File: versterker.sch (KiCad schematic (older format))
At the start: 4 parts, among them J1 J_Barreljack_3.5mm_Wurth_TH

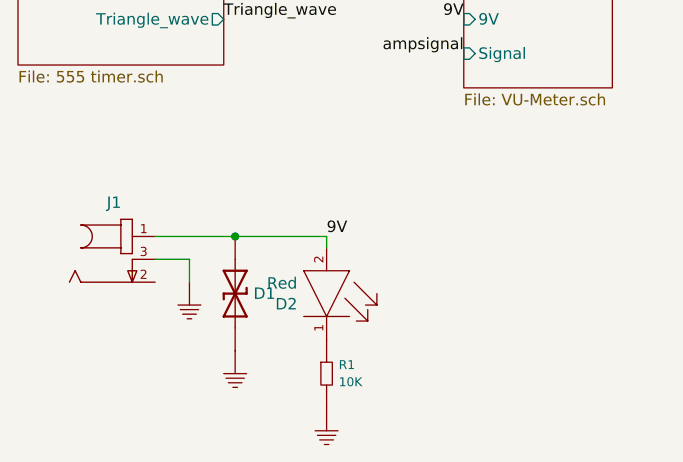
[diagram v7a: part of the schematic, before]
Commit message: changed partnumbers
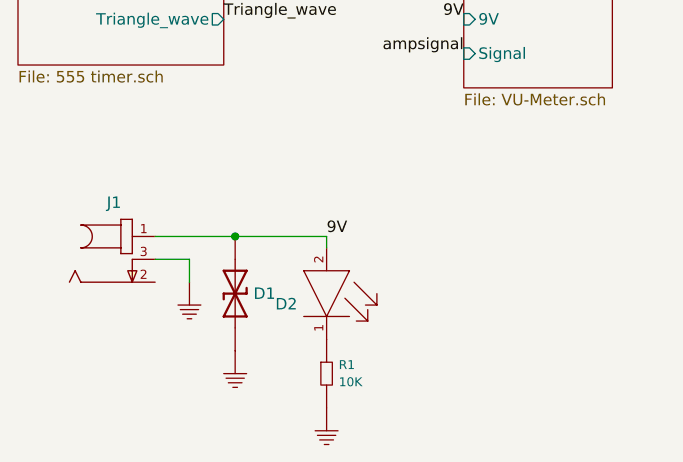
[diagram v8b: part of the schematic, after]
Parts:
- D2: Mouser (none) -> 710-150060RS75000; automotive No -> (none); category Diode -> (none); colour Red -> (none); device class L1 Optoelectronics -> (none); device class L2 LEDs -> (none); device class L3 unset -> (none); digikey description LED RED CLEAR 0603 SMD -> (none); digikey part number 732-4978-1-ND -> (none); forward current 20mA -> (none); forward voltage 2V -> (none); height 0.8mm -> (none); lead free Yes -> (none); led orientation Top View -> (none); library id cd4e03a66a96d806 -> (none); luminous intensity 250mcd -> (none); manufacturer Wurth -> (none); max junction temp +95°C -> (none); mouser description Standard LEDs - SMD WL-SMCW SMDMono TpVw Waterclr 0603 Red -> (none); mouser part number 710-150060RS75000 -> (none); package 0603 -> (none); peak emmision wavelength 630nm -> (none); power dissipation 72mW -> (none); reverse voltage 5V -> (none); rohs Yes -> (none); standoff height 0mm -> (none); temperature range high +85°C -> (none); temperature range low -40°C -> (none); viewing angle 140° -> (none); wavelength 625nm -> (none)
- R1: Digi-key YAG1236CT-ND -> (none); Mouser (none) -> 667-ERJ-UP3F1002V
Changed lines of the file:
@@
 F 2 "MAIN_PCB_LIB:D_9V_TVS_SMCJ-Q" H 3100 4050 50  0001 L BNN
 F 3 "" H 3100 4050 50  0001 L BNN
-F 4 "IPC-7351B" H 3100 4050 50  0001 L BNN "STANDARD"
-F 5 "Diodes Incorporated" H 3100 4050 50  0001 L BNN "MANUFACTURER"
-F 6 "2.62mm" H 3100 4050 50  0001 L BNN "MAXIMUM_PACKAGE_HEIGHT"
-F 7 "11/20/15" H 3100 4050 50  0001 L BNN "PARTREV"
-F 8 "576-SMCJ9.0CA" H 3100 4050 50  0001 C CNN "Mouser"
+F 4 "576-SMCJ9.0CA" H 3100 4050 50  0001 C CNN "Mouser"
+F 5 "Diodes Incorporated" H 0   0   50  0001 C CNN "MANUFACTURER"
+F 6 "2.62mm" H 0   0   50  0001 C CNN "MAXIMUM_PACKAGE_HEIGHT"
+F 7 "11/20/15" H 0   0   50  0001 C CNN "PARTREV"
+F 8 "IPC-7351B" H 0   0   50  0001 C CNN "STANDARD"
 	1    3100 4050
 	0    1    1    0
@@
 F 2 "MAIN_PCB_LIB:D_RED_0603_Wurth" H 3500 4300 50  0001 L CNN
 F 3 "https://www.we-online.com/catalog/datasheet/150060RS75000.pdf" H 3500 4400 50  0001 L CNN
-F 4 "No" H 3500 4500 50  0001 L CNN "automotive"
-F 5 "Diode" H 3500 4600 50  0001 L CNN "category"
-F 6 "Red" V 3755 3572 50  0000 R CNN "colour"
-F 7 "Optoelectronics" H 3500 4800 50  0001 L CNN "device class L1"
-F 8 "LEDs" H 3500 4900 50  0001 L CNN "device class L2"
-F 9 "unset" H 3500 5000 50  0001 L CNN "device class L3"
-F 10 "LED RED CLEAR 0603 SMD" H 3500 5100 50  0001 L CNN "digikey description"
-F 11 "732-4978-1-ND" H 3500 5200 50  0001 L CNN "digikey part number"
-F 12 "20mA" H 3500 5300 50  0001 L CNN "forward current"
-F 13 "2V" H 3500 5400 50  0001 L CNN "forward voltage"
-F 14 "0.8mm" H 3500 5500 50  0001 L CNN "height"
-F 15 "Yes" H 3500 5600 50  0001 L CNN "lead free"
-F 16 "Top View" H 3500 5700 50  0001 L CNN "led orientation"
-F 17 "cd4e03a66a96d806" H 3500 5800 50  0001 L CNN "library id"
-F 18 "250mcd" H 3500 5900 50  0001 L CNN "luminous intensity"
-F 19 "Wurth" H 3500 6000 50  0001 L CNN "manufacturer"
-F 20 "+95°C" H 3500 6100 50  0001 L CNN "max junction temp"
-F 21 "Standard LEDs - SMD WL-SMCW SMDMono TpVw Waterclr 0603 Red" H 3500 6200 50  0001 L CNN "mouser description"
-F 22 "710-150060RS75000" H 3500 6300 50  0001 L CNN "mouser part number"
-F 23 "0603" H 3500 6400 50  0001 L CNN "package"
-F 24 "630nm" H 3500 6500 50  0001 L CNN "peak emmision wavelength"
-F 25 "72mW" H 3500 6600 50  0001 L CNN "power dissipation"
-F 26 "5V" H 3500 6700 50  0001 L CNN "reverse voltage"
-F 27 "Yes" H 3500 6800 50  0001 L CNN "rohs"
-F 28 "0mm" H 3500 6900 50  0001 L CNN "standoff height"
-F 29 "+85°C" H 3500 7000 50  0001 L CNN "temperature range high"
-F 30 "-40°C" H 3500 7100 50  0001 L CNN "temperature range low"
-F 31 "140°" H 3500 7200 50  0001 L CNN "viewing angle"
-F 32 "625nm" H 3500 7300 50  0001 L CNN "wavelength"
+F 4 "710-150060RS75000" H 3500 3700 50  0001 C CNN "Mouser"
 	1    3500 3700
 	0    1    1    0
@@
 F 3 "" H 3450 4500 39  0001 C CNN
 F 4 "10K" H 3553 4313 39  0000 L CNN "Waarde"
-F 5 "YAG1236CT-ND" H 3500 4950 39  0001 C CNN "Digi-key"
+F 5 "667-ERJ-UP3F1002V" H 0   0   50  0001 C CNN "Mouser"
 	1    3500 4350
 	1    0    0    -1
